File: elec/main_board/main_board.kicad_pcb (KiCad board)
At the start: 2 copper layers, 124.7 x 100 mm, 115 parts, among them J1 B2B-PH, J10 Conn_01x02, J11 B2B-XH-A(LF)(SN), J13 B4B-ZR(LF)(SN), J15 GT-USB-7055E, J16 B4B-ZR(LF)(SN), J2 B2B-PH, J3 PSR-41253-06O, J4 PinHeader, J5 PSR-41253-06O, J6 PSR-41253-06O, J7 Conn_01x02, J8 PSR-41253-06O, J9 MJ-179PH, Q1 IRLML6344, Q10 ST-1KL3A, Q11 ST-1KL3A, Q12 ST-1KL3A, Q13 DMT6008LFG, Q2 IRLML6344, Q3 IRLML6344, Q4 IRLML6344, Q5 DMT6008LFG, Q6 DMT6008LFG, Q7 DTC114E, Q8 DTC114E, Q9 ST-1KL3A, SW1 B3U-1000P, SW2 B3U-1000P, U10 AS5047D, U11 LSM6DSR, U12 OKL-T/6-W12N-C, U13 XC6221B332MR, U14 LM74700QDBVRQ1, U15 MCP73213T-A6SI/MF, U16 LM74700QDBVRQ1, U17 FT231XQ-R, U2 BD63573NUV, U5 BD63573NUV, U6 ESP32-S3-WROOM-1, U9 AS5047D

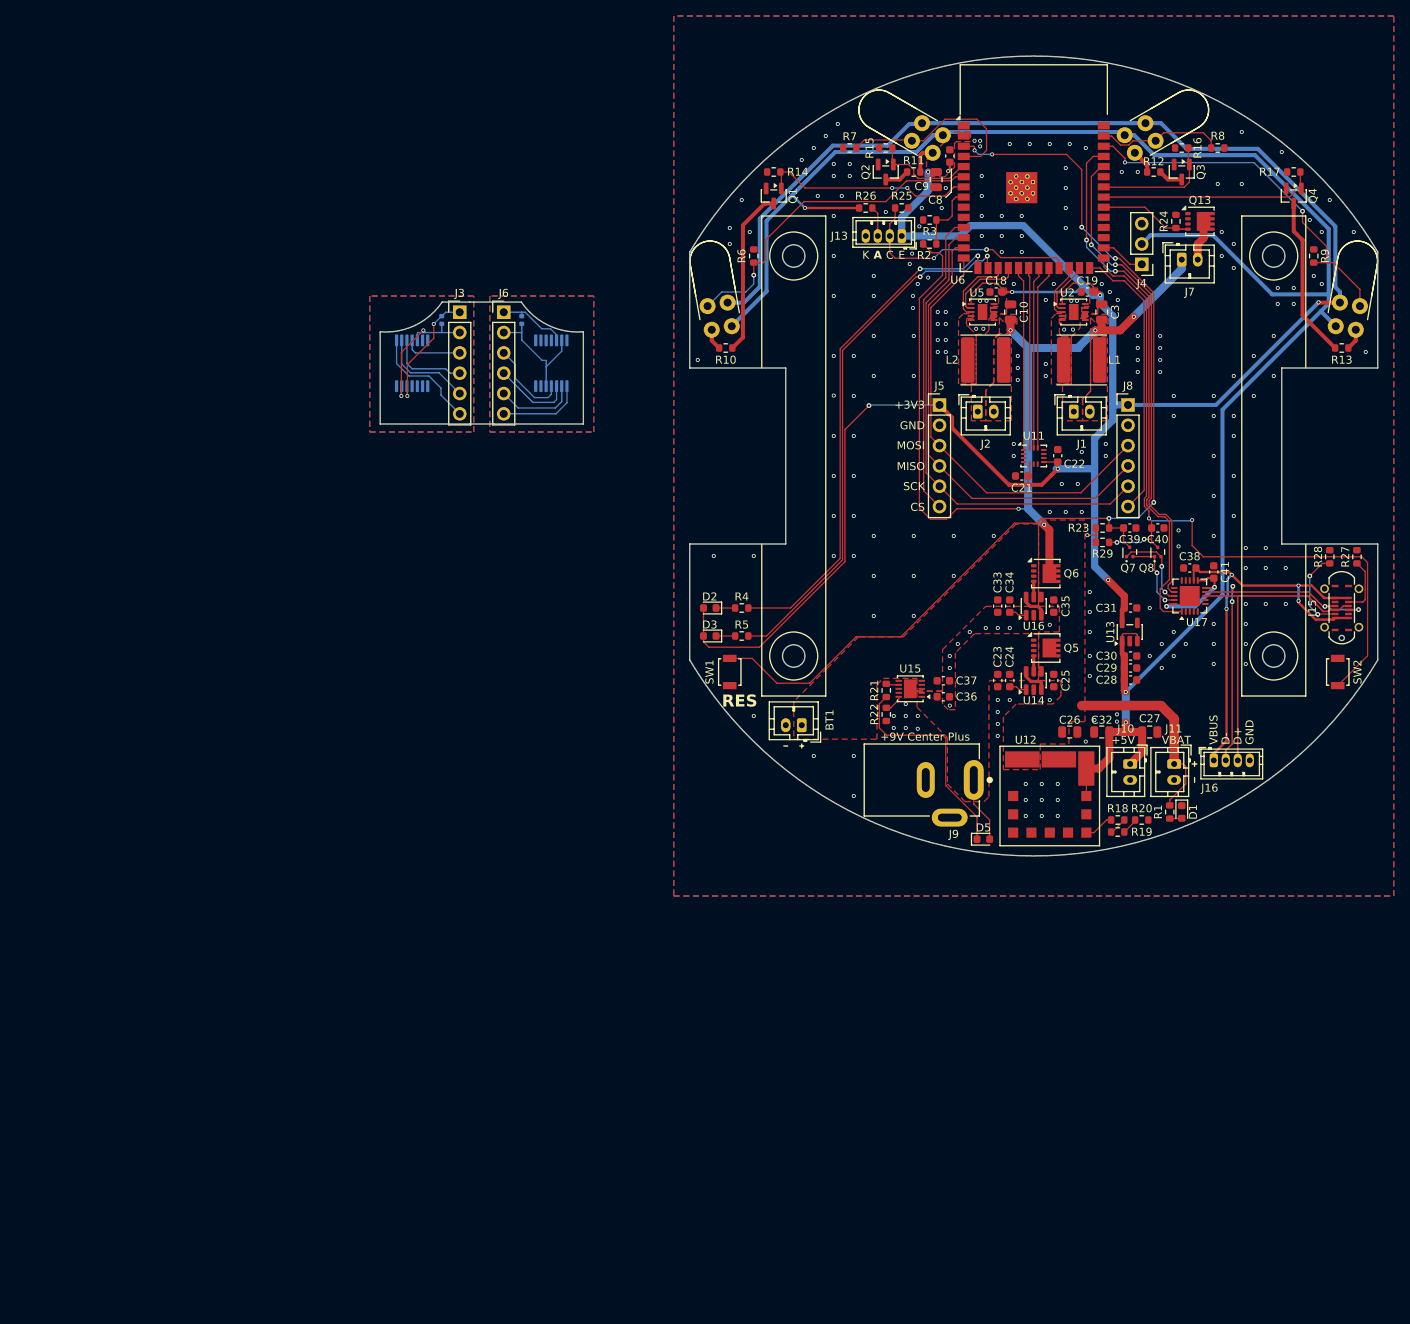
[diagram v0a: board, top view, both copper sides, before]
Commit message: 再設計　部品配置完了
Signed-off-by: Kazuki Iida <elkel53930@gmail.com>
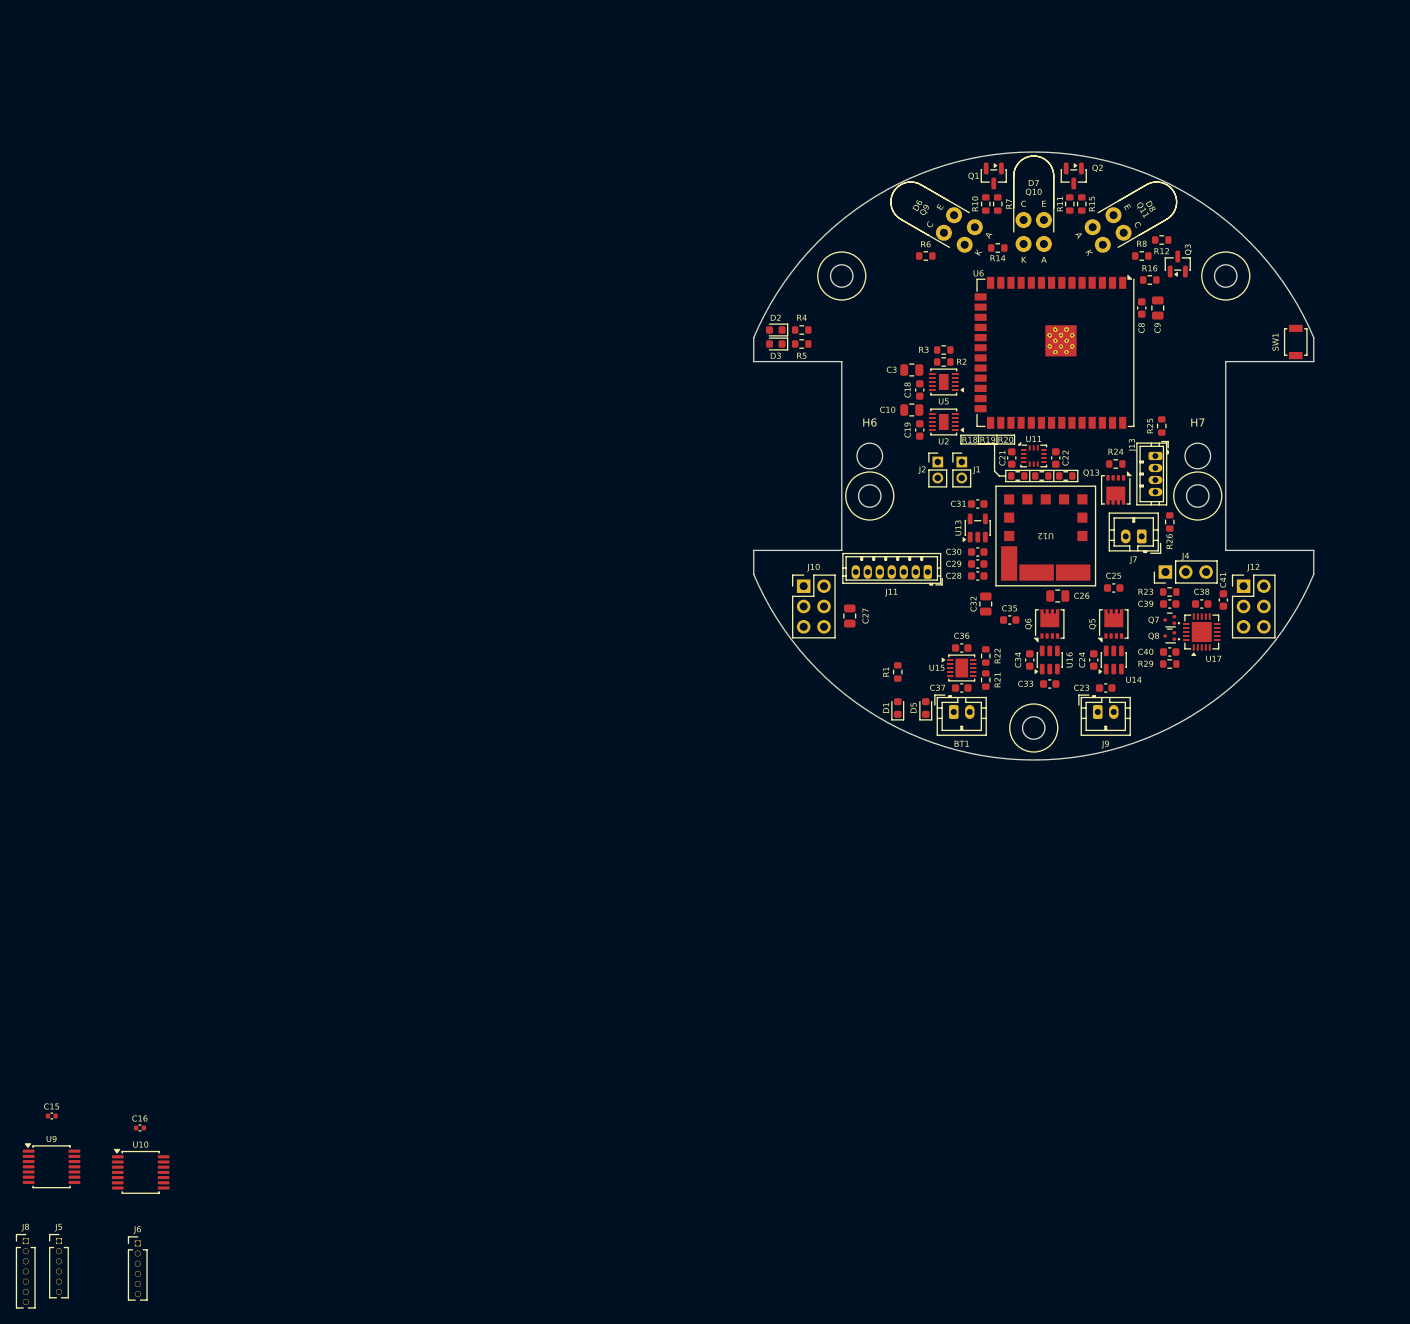
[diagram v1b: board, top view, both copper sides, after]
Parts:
- removed D9: SFH4550, Library:SFH4550_Mirror
- removed G***: LOGO, Library:AMacLogo
- removed J15: GT-USB-7055E, Library:USB-C-SMD_GT-USB-7055E
- removed J16: B4B-ZR(LF)(SN), Connector_JST:JST_ZH_B4B-ZR_1x04_P1.50mm_Vertical
- removed J3: PSR-41253-06O, Connector_PinHeader_2.54mm:PinHeader_1x06_P2.54mm_Vertical
- removed L1, L2: NR6045T100M, Inductor_SMD:L_Changjiang_FNR6040S
- removed Q12: ST-1KL3A, Library:ST-1KL3A_Mirror
- removed Q4: IRLML6344, Package_TO_SOT_SMD:SOT-23
- removed R13: 0603WAF1000T5E, Resistor_SMD:R_0603_1608Metric
- removed R17: 0603WAF1002T5E, Resistor_SMD:R_0603_1608Metric
- removed R27, R28: 0603WAF5101T5E, Resistor_SMD:R_0603_1608Metric
- removed R9: 0603WAF4700T5E, Resistor_SMD:R_0603_1608Metric
- removed SW2: B3U-1000P, Button_Switch_SMD:SW_SPST_B3U-1000P
- added H5: M2.6 mounting hole, Library:M2.6 Mounting Hole, F.Cu at (119.5, 95.0)
- added H6: M3 mounting hole, MountingHole:MountingHole_3.2mm_M3, F.Cu at (119.5, 90.0)
- added H7: M3 mounting hole, MountingHole:MountingHole_3.2mm_M3, F.Cu at (160.5, 90.0)
- added J12: FSS-42085-03, Connector_PinHeader_2.54mm:PinHeader_2x03_P2.54mm_Vertical, F.Cu at (166.2, 106.3)
- BT1: value 800mAh LiPo 2S -> B2B-PH
- C15, C16, U10, U9: moved to F.Cu
- J1, J2: value B2B-PH -> Motor; footprint Connector_JST:JST_PH_B2B-PH-K_1x02_P2.00mm_Vertical -> Connector_PinHeader_2.00mm:PinHeader_1x02_P2.00mm_Vertical
- J10: value Conn_01x02 -> FSS-42085-03; footprint Connector_JST:JST_PH_B2B-PH-K_1x02_P2.00mm_Vertical -> Connector_PinHeader_2.54mm:PinHeader_2x03_P2.54mm_Vertical
- J11: value B2B-XH-A(LF)(SN) -> B7B-ZR; footprint Connector_JST:JST_PH_B2B-PH-K_1x02_P2.00mm_Vertical -> Connector_JST:JST_ZH_B7B-ZR_1x07_P1.50mm_Vertical
- J5, J6: footprint Connector_PinHeader_2.54mm:PinHeader_1x06_P2.54mm_Vertical -> Connector_PinHeader_1.27mm:PinHeader_1x06_P1.27mm_Vertical
- J8: value PSR-41253-06O -> Conn_01x07_Pin; footprint Connector_PinHeader_2.54mm:PinHeader_1x06_P2.54mm_Vertical -> Connector_PinHeader_1.27mm:PinHeader_1x07_P1.27mm_Vertical
- J9: value MJ-179PH -> B2B-PH; footprint Library:PJ-002A -> Connector_JST:JST_PH_B2B-PH-K_1x02_P2.00mm_Vertical
- U6: value ESP32-S3-WROOM-1 -> ESP32-S3-WROOM-1U; footprint RF_Module:ESP32-S3-WROOM-1 -> RF_Module:ESP32-S3-WROOM-1U
- moved J8 172.9 mm to (14.0, 188.1)
- moved J5 151.8 mm to (18.1, 188.1)
- moved J6 125.1 mm to (28.0, 188.4)
- moved U10 113.4 mm to (28.4, 179.6), turned to 0 degrees
- moved C16 111.7 mm to (28.3, 174.0), turned to 0 degrees
- moved C15 110.8 mm to (17.2, 172.5), turned to 0 degrees
- moved U9 110.1 mm to (17.2, 178.8), turned to 0 degrees
- moved SW1 81.9 mm to (172.8, 75.8)
- moved H2 71.9 mm to (164.0, 67.5)
- moved H1 58.7 mm to (160.5, 95.0)
- moved R26 54.6 mm to (157.0, 98.2), turned to -90 degrees
- moved H3 54.1 mm to (116.0, 67.5)
- moved J10 46.5 mm to (111.2, 106.3), turned to 0 degrees
- moved R19 45.5 mm to (141.0, 92.5)
- moved R18 44.8 mm to (138.0, 92.5)
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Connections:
- net Net-(J6-Pin_1) renamed /ENCR__3V3
- net Net-(J6-Pin_2) renamed /ENCR_GND
- net Net-(J6-Pin_3) renamed /ENCR_MOSI
- net Net-(J6-Pin_4) renamed /ENCR_MISO
- net Net-(J6-Pin_5) renamed /ENCR_SCK
- net Net-(J6-Pin_6) renamed /ENCR_CS_R
- C15 pad 1: Net-(J3-Pin_2) -> /ENCL_GND
- C15 pad 2: Net-(J3-Pin_1) -> /ENCL__3V3
- C38 pad 2: VBUS -> +5V
- J10 pad 1: +5V -> +BATT
- J10 pad 2: GND -> +BATT
- J11 pad 1: +BATT -> +3V3
- J5 pad 1: +3V3 -> /ENCL__3V3
- J5 pad 2: GND -> /ENCL_GND
- J5 pad 3: /SPI1_MOSI -> /ENCL_MOSI
- J5 pad 4: /SPI1_MISO -> /ENCL_MISO
- J5 pad 5: /SPI1_SCK -> /ENCL_SCK
- J5 pad 6: /CS_ENC_L -> /ENCL_CS_R
- J8 pad 1: +3V3 -> /ENCL__3V3
- J8 pad 2: GND -> /ENCL_GND
- J8 pad 3: /SPI1_MOSI -> /ENCL_MOSI
- J8 pad 4: /SPI1_MISO -> /ENCL_MISO
- J8 pad 5: /SPI1_SCK -> /ENCL_SCK
- J8 pad 6: /CS_ENC_R -> /ENCL_CS_L
- Q1 pad 1: /LF_EN -> /L_EN
- Q10 pad 1: /LS_SEN -> /F_SEN
- Q11 pad 1: /RS_SEN -> /R_SEN
- Q2 pad 1: /LS_EN -> /F_EN
- Q3 pad 1: /RS_EN -> /R_EN
- Q9 pad 1: /LF_SEN -> /L_SEN
- R14 pad 2: /LF_EN -> /L_EN
- R15 pad 2: /LS_EN -> /F_EN
- R16 pad 2: /RS_EN -> /R_EN
- R6 pad 2: /LF_SEN -> /L_SEN
- R7 pad 2: /LS_SEN -> /F_SEN
- R8 pad 2: /RS_SEN -> /R_SEN
- U17 pad 12: VBUS -> +5V
- U17 pad 8: /Power/USB+ -> /Power/USB_DP
- U17 pad 9: /Power/USB- -> /Power/USB_DM
- U2 pad 4: Net-(U2-OUTB) -> Net-(J1-Pin_2)
- U5 pad 4: Net-(U5-OUTB) -> Net-(J2-Pin_2)
- U6 pad 11: /CS_ENC_L -> unconnected-(U6-IO18-Pad11)
- U6 pad 12: /SPI1_SCK -> unconnected-(U6-IO8-Pad12)
- U6 pad 13: /SPI1_MISO -> /LED_0
- U6 pad 14: /SPI1_MOSI -> /LED_1
- U6 pad 15: /LED_0 -> unconnected-(U6-IO3-Pad15)
- U6 pad 16: /LED_1 -> /CS_ENC_R
- U6 pad 17: /PWM_L -> /CS_ENC_L
- U6 pad 18: /CWCCW_L -> /SPI1_SCK
- U6 pad 19: /SPI2_MISO -> /SPI1_MISO
- U6 pad 20: /SPI2_MOSI -> /SPI1_MOSI
- U6 pad 21: /SPI2_SCK -> /BAT_MON
- U6 pad 22: /CS_IMU -> /BALL_DET
- U6 pad 23: /BALL_DET -> /PWM_L
- U6 pad 24: /PWM_R -> /CWCCW_L
- U6 pad 25: /CWCCW_R -> /PWM_R
- U6 pad 26: /CS_ENC_R -> /CWCCW_R
- U6 pad 28: /SERVO_SIG1 -> unconnected-(U6-IO35-Pad28)
- U6 pad 31: unconnected-(U6-IO38-Pad31) -> /SPI2_MISO
- U6 pad 32: /PWM_FAN -> /SPI2_MOSI
- U6 pad 33: /RF_EN -> /SPI2_SCK
- U6 pad 34: /RS_EN -> /CS_IMU
- U6 pad 38: /RF_SEN -> /PWM_FAN
- U6 pad 39: /RS_SEN -> /SERVO_SIG1
- U6 pad 4: /LS_SEN -> /R_EN
- U6 pad 5: /LS_EN -> /R_SEN
- U6 pad 6: /LF_SEN -> /F_EN
- U6 pad 7: /LF_EN -> /F_SEN
- U6 pad 8: /BAT_MON -> /L_EN
- U6 pad 9: unconnected-(U6-IO16-Pad9) -> /L_SEN
- U9 pad 1: Net-(J3-Pin_6) -> /ENCL_CS_L
- U9 pad 12: Net-(J3-Pin_1) -> /ENCL__3V3
- U9 pad 13: Net-(J3-Pin_2) -> /ENCL_GND
- U9 pad 2: Net-(J3-Pin_5) -> /ENCL_SCK
- U9 pad 3: Net-(J3-Pin_4) -> /ENCL_MISO
- U9 pad 4: Net-(J3-Pin_3) -> /ENCL_MOSI
- U9 pad 5: Net-(J3-Pin_2) -> /ENCL_GND
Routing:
- net +3V3: track 338.2 -> 0.00 mm, vias 8 -> 0
- net +5V: track 235.8 -> 0.00 mm, vias 3 -> 0
- net +BATT: track 135.2 -> 0.00 mm, vias 5 -> 0
- net CHIP_PU: track 131.4 -> 0.00 mm, vias 6 -> 0
- net GPIO0: track 94.0 -> 0.00 mm, vias 4 -> 0
- net TXD0: track 67.4 -> 0.00 mm, vias 2 -> 0
- net /LED_1: track 66.4 -> 0.00 mm, vias 2 -> 0
- net /LED_0: track 63.8 -> 0.00 mm, vias 2 -> 0
- net RXD0: track 60.3 -> 0.00 mm, vias 2 -> 0
- net /SPI1_SCK: track 59.7 -> 0.00 mm
- net /SPI1_MISO: track 57.2 -> 0.00 mm
- net VBUS: track 55.7 -> 0.00 mm, vias 4 -> 0
- net /SPI1_MOSI: track 54.0 -> 0.00 mm
- net /Power/USB-: track 45.9 -> 0.00 mm, vias 4 -> 0
- net /RF_SEN: track 45.4 -> 0.00 mm, vias 2 -> 0
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- removed copper zone on F.Cu, net +3V3
- removed copper zone on F.Cu, net +BATT
- removed copper zone on B.Cu, net /ENCR_GND
- removed copper zone on F.Cu, net /ENCR_GND
- removed copper zone on F.Cu, net /Power/EXT_PWR
- removed copper zone on B.Cu, net GND
- removed copper zone on F.Cu, net GND
- removed copper zone on F.Cu, net Net-(BT1-+)
- removed copper zone on F.Cu, net Net-(J1-Pin_1)
- removed copper zone on F.Cu, net Net-(J1-Pin_2)
- removed copper zone on F.Cu, net Net-(J2-Pin_1)
- removed copper zone on F.Cu, net Net-(J2-Pin_2)
- removed copper zone on B.Cu, net Net-(J3-Pin_2)
- removed copper zone on F.Cu, net Net-(J3-Pin_2)
- removed copper zone on F.Cu, net Net-(U2-OUTB)
- removed copper zone on F.Cu, net Net-(U5-OUTB)
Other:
- board size 124.7 x 100 mm -> 70 x 76 mm
- board text removed: "+3V3"
- board text removed: "+5V"
- board text removed: "+9V Center Plus"
- board text removed: "A"
- board text removed: "C"
- board text removed: "CS"
- board text removed: "D+"
- board text removed: "D-"
- board text removed: "E"
- board text removed: "GND"
- board text removed: "K"
- board text removed: "MISO"
- board text removed: "MOSI"
- board text removed: "RES"
- board text removed: "RoboSweep Agent 2026 Daylight"
- board text removed: "SCK"
- board text removed: "VBAT"
- board text removed: "VBUS"

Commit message: 配線作業中
Signed-off-by: Kazuki Iida <elkel53930@gmail.com>
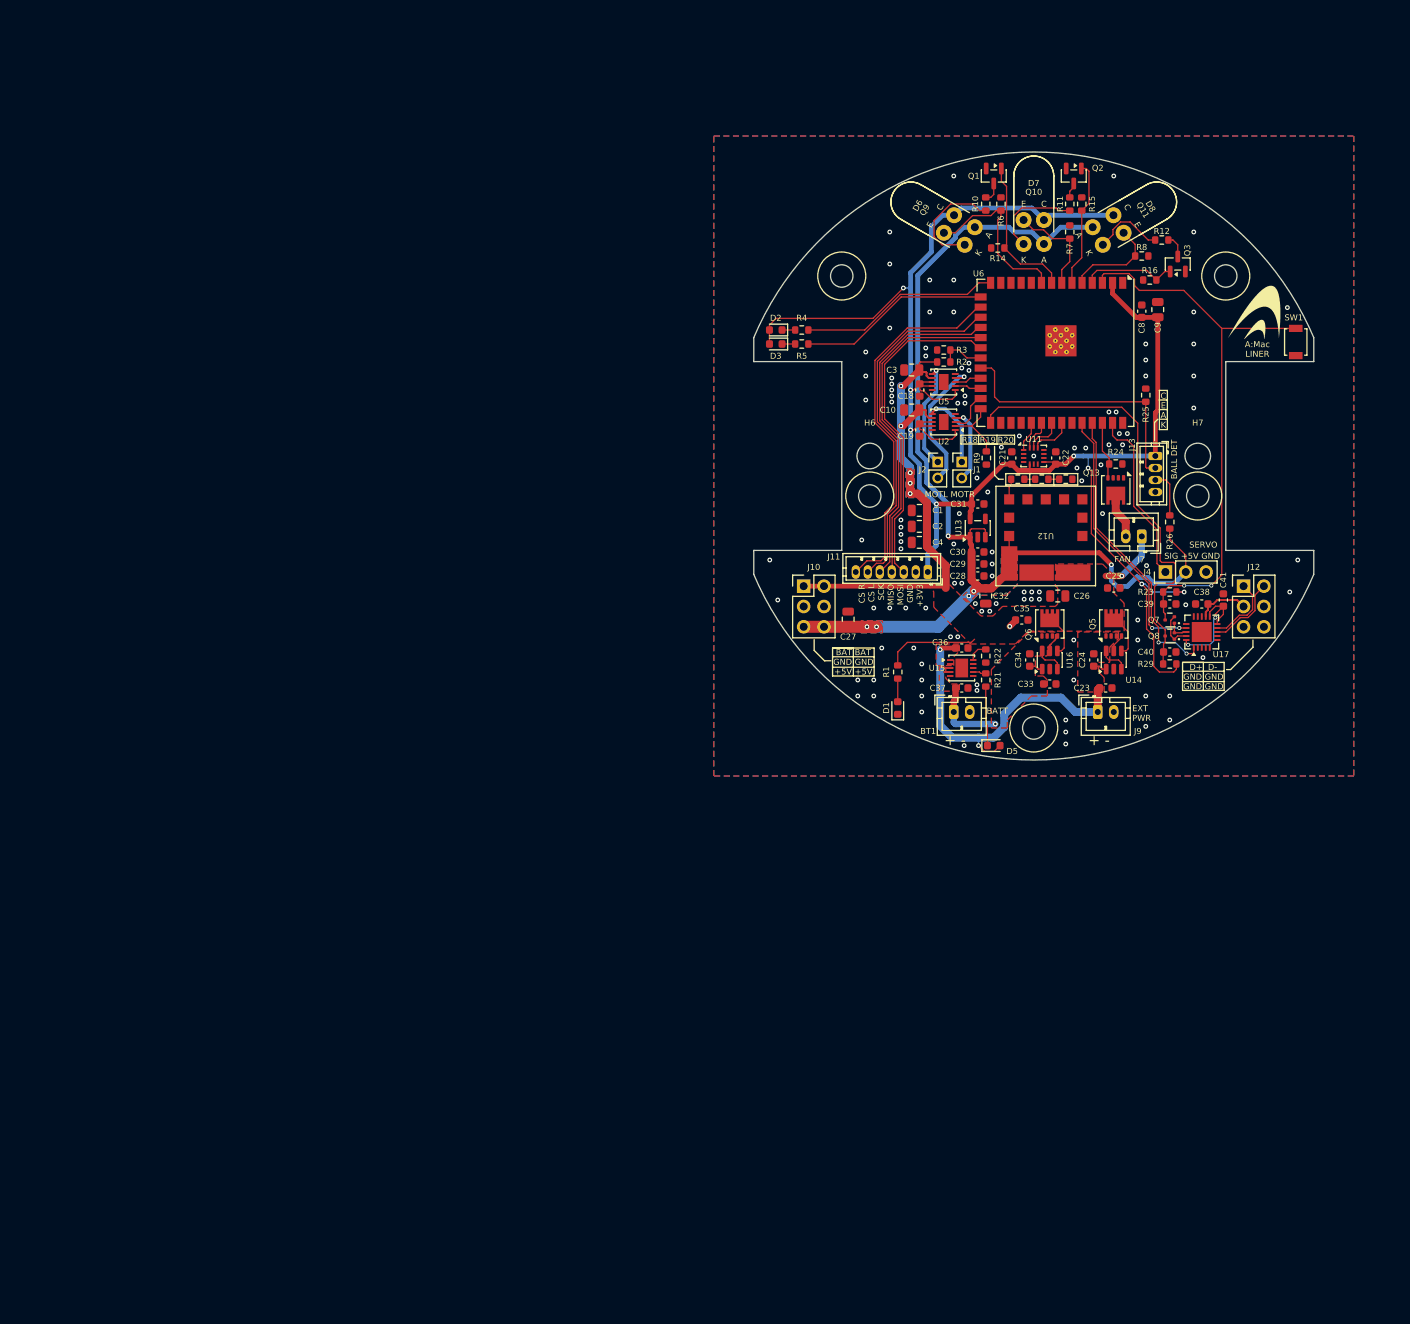
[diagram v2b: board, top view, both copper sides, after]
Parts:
- removed C15: CC0603KRX7R9BB104, Capacitor_SMD:C_0402_1005Metric
- removed C16: CL05B104KO5NNNC, Capacitor_SMD:C_0402_1005Metric
- removed J5, J6: PSR-41253-06O, Connector_PinHeader_1.27mm:PinHeader_1x06_P1.27mm_Vertical
- removed J8: Conn_01x07_Pin, Connector_PinHeader_1.27mm:PinHeader_1x07_P1.27mm_Vertical
- removed U10, U9: AS5047D, Package_SO:TSSOP-14_4.4x5mm_P0.65mm
- added C1: CL21A106KAYNNNE, Capacitor_SMD:C_0805_2012Metric, F.Cu at (125.7, 96.8)
- added C2: CL21A106KAYNNNE, Capacitor_SMD:C_0805_2012Metric, F.Cu at (125.7, 98.8)
- added C4: CL21A106KAYNNNE, Capacitor_SMD:C_0805_2012Metric, F.Cu at (125.7, 100.8)
- added G***: LOGO, Library:AMacLogo, F.Cu at (167.2, 72.0)
- added G***: LOGO, Library:AMacLogo, B.Cu at (141.0, 81.0)
- added R9: 0603WAF1002T5E, Resistor_SMD:R_0603_1608Metric, F.Cu at (134.1, 90.2)
- C39: value CC0603KRX7R9BB104 -> CL10A105KB8NNNC
- moved R6 11.4 mm to (135.9, 58.5), turned to -90 degrees
- moved D5 9.71 mm to (135.0, 126.2), turned to 0 degrees
- moved R7 9.66 mm to (144.5, 62.0)
- moved R25 4.34 mm to (154.0, 82.4)
- moved C35 1.50 mm to (138.5, 110.5)
- moved C32 1.00 mm to (134.0, 107.5)
- moved C27 0.45 mm to (116.8, 110.4)
- moved C8 0.40 mm to (153.5, 71.9), turned to -90 degrees
- moved R18 0.40 mm to (138.0, 92.9)
- moved R19 0.40 mm to (141.0, 92.9)
- moved R20 0.40 mm to (144.0, 92.9)
- moved C9 0.20 mm to (155.5, 71.7), turned to -90 degrees
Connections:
- C38 pad 2: +5V -> VBUS
- J12 pad 3: GND -> VBUS
- U17 pad 12: +5V -> VBUS
- U6 pad 13: /LED_0 -> unconnected-(U6-USB_D--Pad13)
- U6 pad 14: /LED_1 -> /LED_0
- U6 pad 15: unconnected-(U6-IO3-Pad15) -> /LED_1
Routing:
- net +3V3: track 0.00 -> 216.8 mm, vias 0 -> 8
- net +5V: track 0.00 -> 140.7 mm, vias 0 -> 6
- net +BATT: track 0.00 -> 93.4 mm, vias 0 -> 6
- net CHIP_PU: track 0.00 -> 71.1 mm, vias 0 -> 2
- net GPIO0: track 0.00 -> 56.4 mm
- net /Power/EXT_PWR: track 0.00 -> 46.7 mm, vias 0 -> 2
- net /CS_ENC_R: track 0.00 -> 46.4 mm
- net /CS_ENC_L: track 0.00 -> 44.5 mm
- net /SPI1_SCK: track 0.00 -> 42.6 mm
- net /SPI1_MOSI: track 0.00 -> 41.4 mm
- net /SPI1_MISO: track 0.00 -> 41.2 mm
- net TXD0: track 0.00 -> 36.6 mm, vias 0 -> 2
- net /BALL_DET: track 0.00 -> 33.7 mm
- net RXD0: track 0.00 -> 33.5 mm, vias 0 -> 2
- net /LED_0: track 0.00 -> 25.2 mm
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- added copper zone on B.Cu, net +5V
- added copper zone on F.Cu, net +5V
- added copper zone on B.Cu, net +BATT
- added copper zone on F.Cu, net +BATT
- added copper zone on F.Cu, net /Power/EXT_PWR
- added copper zone on B.Cu, net GND
- added copper zone on F.Cu, net GND
- added copper zone on F.Cu, net Net-(BT1-+)
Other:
- board text added: "+ -"
- board text added: "A:Mac LINER"
- board text added: "BALL DET"
- board text added: "BAT BAT GND GND +5V +5V"
- board text added: "BATT"
- board text added: "C E A K"
- board text added: "CS R CS L SCK MISO MOSI GND +3V3"
- board text added: "D+ D- GND GND GND GND"
- board text added: "EXT PWR"
- board text added: "FAN"
- board text added: "MOTL MOTR"
- board text added: "RoboSweep Agent LINER"
- board text added: "SERVO"
- board text added: "SIG +5V GND"
- board text added: "ver 1.0"

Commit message: アートワーク完了、発注
Signed-off-by: Kazuki Iida <elkel53930@gmail.com>
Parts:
- moved G*** 2.15 mm to (167.2, 74.1)
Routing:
- net +BATT: track 93.4 -> 91.7 mm
- net GPIO0: track 56.4 -> 55.8 mm
- net GND: vias 112 -> 113
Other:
- board text added: "ver 1.0 2026.06"
- board text removed: "A:Mac LINER"
- board text removed: "ver 1.0"
